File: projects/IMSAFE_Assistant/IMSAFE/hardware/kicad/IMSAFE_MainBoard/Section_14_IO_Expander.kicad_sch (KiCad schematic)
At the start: 6 parts, among them U16 MCP23017-E/SO

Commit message: Fix ERC errors across multiple schematic sections
- Section_04_BMS: Add VSYS hierarchical label for root schematic connection
- Section_05/06 Regulators: Add PWR_FLAG wire and junction to VSYS net
- Section_07_Barometric: Connect BMP390 SCK pin to GND for I2C mode
- Section_14_IO_Expander: Add no-connect symbols for unused MCP23017 GPIO pins
- Update design-rationale.md with ERC remediation status

Co-Authored-By: Claude Opus 4.5 <noreply@anthropic.com>
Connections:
- no-connect marks 0 -> 16
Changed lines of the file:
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@@
 	(wire (pts (xy 139.7 109.22) (xy 147.32 109.22)) (stroke (width 0) (type default)) (uuid "w-hl-inta"))
 	(wire (pts (xy 139.7 106.68) (xy 147.32 106.68)) (stroke (width 0) (type default)) (uuid "w-hl-intb"))
+	(no_connect (at 114.3 124.46) (uuid "nc-gpb0"))
+	(no_connect (at 114.3 121.92) (uuid "nc-gpb1"))
+	(no_connect (at 114.3 83.82) (uuid "nc-gpb2"))
+	(no_connect (at 114.3 86.36) (uuid "nc-gpb3"))
+	(no_connect (at 114.3 91.44) (uuid "nc-gpb4"))
+	(no_connect (at 114.3 93.98) (uuid "nc-gpb5"))
+	(no_connect (at 114.3 96.52) (uuid "nc-gpb6"))
+	(no_connect (at 114.3 99.06) (uuid "nc-gpb7"))
+	(no_connect (at 114.3 101.6) (uuid "nc-gpa0"))
+	(no_connect (at 114.3 104.14) (uuid "nc-gpa1"))
+	(no_connect (at 139.7 83.82) (uuid "nc-gpa2"))
+	(no_connect (at 139.7 86.36) (uuid "nc-gpa3"))
+	(no_connect (at 139.7 91.44) (uuid "nc-gpa4"))
+	(no_connect (at 139.7 93.98) (uuid "nc-gpa5"))
+	(no_connect (at 139.7 96.52) (uuid "nc-gpa6"))
+	(no_connect (at 139.7 99.06) (uuid "nc-gpa7"))
 	(sheet_instances (path "/" (page "1")))
 )

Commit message: Fix additional ERC errors in regulator and IO expander sections
- Section_05/06: Remove redundant PWR_FLAG on VSYS (BMS provides power_output)
- Section_14: Correct MCP23017 NC symbol positions to match actual pin coordinates

ERC reduction: 412 → 390 violations (22 fewer)
- Errors: 150 → 129 (-21)
- Warnings: 262 → 261 (-1)

Co-Authored-By: Claude Opus 4.5 <noreply@anthropic.com>
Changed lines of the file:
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@@
 	(no_connect (at 114.3 124.46) (uuid "nc-gpb0"))
 	(no_connect (at 114.3 121.92) (uuid "nc-gpb1"))
-	(no_connect (at 114.3 83.82) (uuid "nc-gpb2"))
-	(no_connect (at 114.3 86.36) (uuid "nc-gpb3"))
-	(no_connect (at 114.3 91.44) (uuid "nc-gpb4"))
-	(no_connect (at 114.3 93.98) (uuid "nc-gpb5"))
-	(no_connect (at 114.3 96.52) (uuid "nc-gpb6"))
-	(no_connect (at 114.3 99.06) (uuid "nc-gpb7"))
+	(no_connect (at 114.3 119.38) (uuid "nc-gpb2"))
+	(no_connect (at 114.3 116.84) (uuid "nc-gpb3"))
+	(no_connect (at 114.3 114.3) (uuid "nc-gpb4"))
+	(no_connect (at 114.3 111.76) (uuid "nc-gpb5"))
+	(no_connect (at 114.3 109.22) (uuid "nc-gpb6"))
+	(no_connect (at 114.3 106.68) (uuid "nc-gpb7"))
 	(no_connect (at 114.3 101.6) (uuid "nc-gpa0"))
-	(no_connect (at 114.3 104.14) (uuid "nc-gpa1"))
-	(no_connect (at 139.7 83.82) (uuid "nc-gpa2"))
-	(no_connect (at 139.7 86.36) (uuid "nc-gpa3"))
-	(no_connect (at 139.7 91.44) (uuid "nc-gpa4"))
-	(no_connect (at 139.7 93.98) (uuid "nc-gpa5"))
-	(no_connect (at 139.7 96.52) (uuid "nc-gpa6"))
-	(no_connect (at 139.7 99.06) (uuid "nc-gpa7"))
+	(no_connect (at 114.3 99.06) (uuid "nc-gpa1"))
+	(no_connect (at 114.3 96.52) (uuid "nc-gpa2"))
+	(no_connect (at 114.3 93.98) (uuid "nc-gpa3"))
+	(no_connect (at 114.3 91.44) (uuid "nc-gpa4"))
+	(no_connect (at 114.3 88.9) (uuid "nc-gpa5"))
+	(no_connect (at 114.3 86.36) (uuid "nc-gpa6"))
+	(no_connect (at 114.3 83.82) (uuid "nc-gpa7"))
 	(sheet_instances (path "/" (page "1")))
 )

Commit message: Add sensor and interface schematic implementations
- Section 01: MCU Core additional connections
- Section 04: BMS refinements
- Section 07: Barometric sensor (BMP390)
- Section 08: IMU (ICM-42688-P) full implementation
- Section 09: Magnetometer (MMC5983MA) full implementation
- Section 10: Gas sensor (MICS-4514) with heater control
- Section 11: Temp/Humidity (Si7021-A20) implementation
- Section 14: I/O Expander updates
- Section 16: Rotary encoder connections
- Section 19: Audio buzzer (MLT-8530) with MOSFET driver

Co-Authored-By: Claude Opus 4.5 <noreply@anthropic.com>
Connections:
- net +3V3: now also R1404.2
- net GND: now also R1401.2
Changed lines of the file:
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@@
 		(instances (project "IMSAFE_MainBoard" (path "/sec14-0001-0002-0003-000000000001" (reference "#PWR01404") (unit 1))))
+	)
+	(symbol (lib_id "power:+3V3") (at 167.64 111.76 90) (unit 1)
+		(exclude_from_sim no) (in_bom yes) (on_board yes) (dnp no)
+		(uuid "pwr-3v3-reset")
+		(property "Reference" "#PWR01405" (at 171.45 111.76 0) (effects (font (size 1.27 1.27)) hide))
+		(property "Value" "+3V3" (at 172.72 111.76 0) (effects (font (size 1.27 1.27))))
+		(property "Footprint" "" (at 167.64 111.76 0) (effects (font (size 1.27 1.27)) hide))
+		(property "Datasheet" "" (at 167.64 111.76 0) (effects (font (size 1.27 1.27)) hide))
+		(pin "1" (uuid "pwr-3v3-reset-p1"))
+		(instances (project "IMSAFE_MainBoard" (path "/sec14-0001-0002-0003-000000000001" (reference "#PWR01405") (unit 1))))
 	)
 	(wire (pts (xy 127 71.12) (xy 127 78.74)) (stroke (width 0) (type default)) (uuid "w-3v3-vdd"))
@@
 	(wire (pts (xy 160.02 92.71) (xy 160.02 96.52)) (stroke (width 0) (type default)) (uuid "w-c1401-gnd"))
 	(wire (pts (xy 139.7 111.76) (xy 151.13 111.76)) (stroke (width 0) (type default)) (uuid "w-reset-r1404"))
-	(wire (pts (xy 158.75 111.76) (xy 165.1 111.76)) (stroke (width 0) (type default)) (uuid "w-r1404-3v3"))
+	(wire (pts (xy 158.75 111.76) (xy 167.64 111.76)) (stroke (width 0) (type default)) (uuid "w-r1404-3v3"))
 	(wire (pts (xy 139.7 88.9) (xy 151.13 88.9)) (stroke (width 0) (type default)) (uuid "w-a0-r1401"))
 	(wire (pts (xy 158.75 88.9) (xy 165.1 88.9)) (stroke (width 0) (type default)) (uuid "w-r1401-gnd"))
@@
 	(wire (pts (xy 139.7 124.46) (xy 151.13 124.46)) (stroke (width 0) (type default)) (uuid "w-a2-r1403"))
 	(wire (pts (xy 158.75 124.46) (xy 165.1 124.46)) (stroke (width 0) (type default)) (uuid "w-r1403-gnd"))
-	(wire (pts (xy 165.1 88.9) (xy 165.1 111.76)) (stroke (width 0) (type default)) (uuid "w-gnd-tie1"))
+	(wire (pts (xy 165.1 88.9) (xy 165.1 121.92)) (stroke (width 0) (type default)) (uuid "w-gnd-tie1"))
 	(wire (pts (xy 165.1 121.92) (xy 165.1 124.46)) (stroke (width 0) (type default)) (uuid "w-gnd-tie2"))
 	(hierarchical_label "I2C1_SDA" (shape bidirectional) (at 147.32 119.38 0) (fields_autoplaced yes)

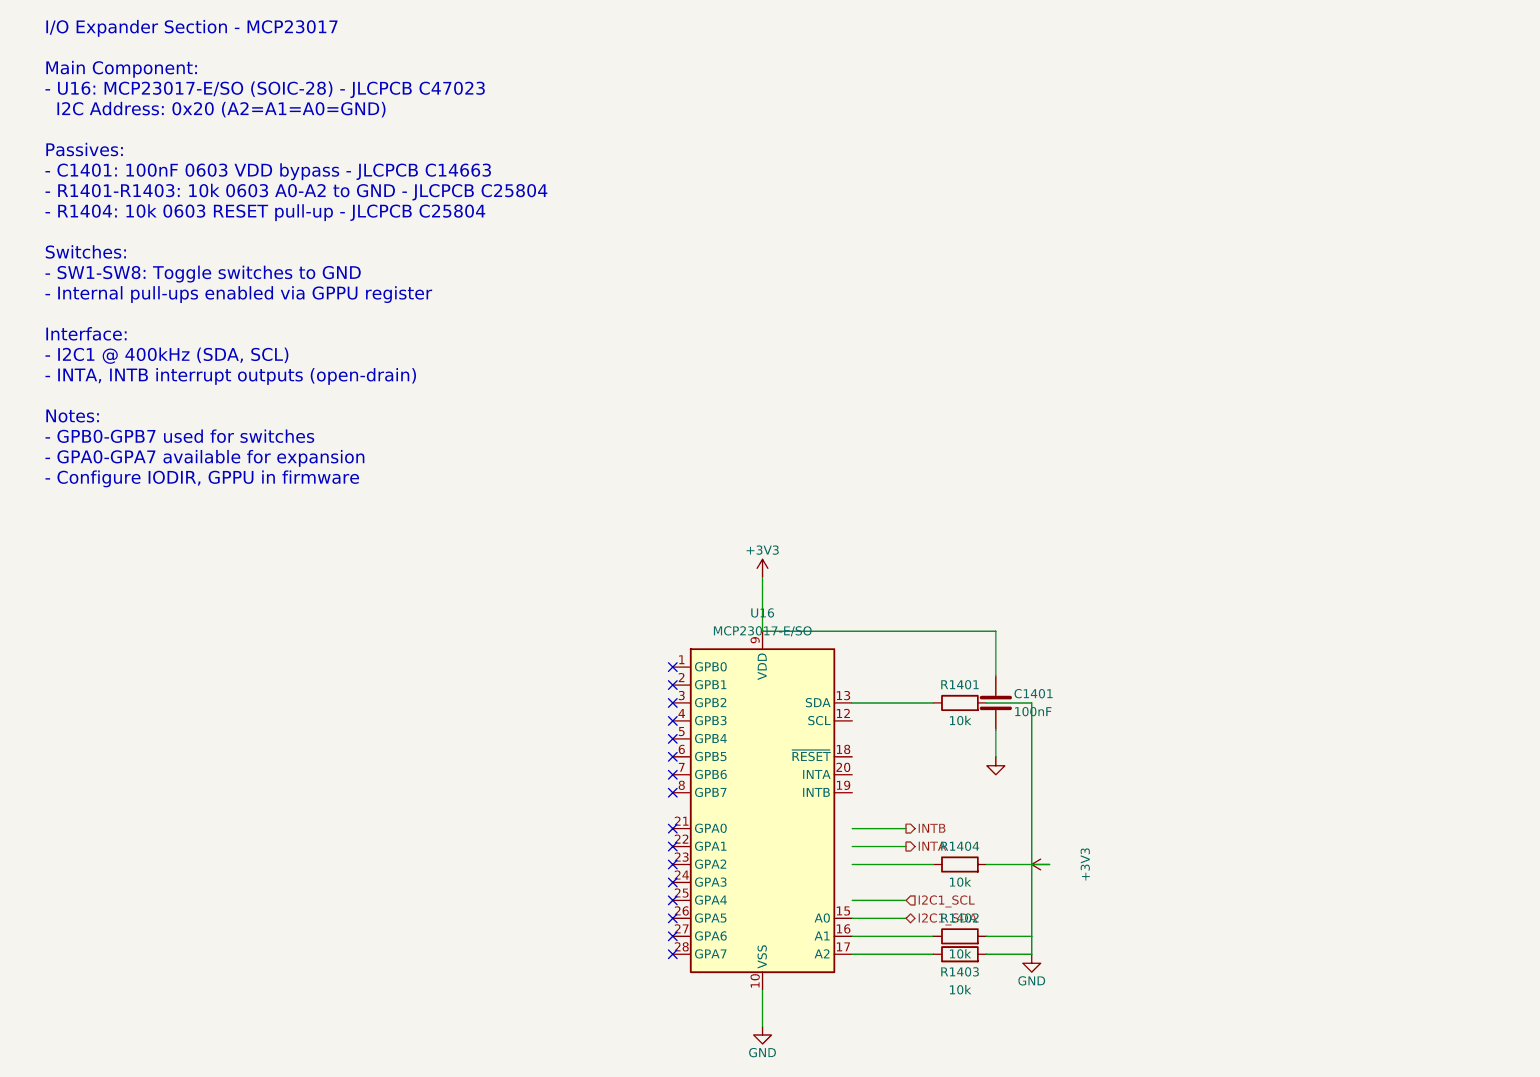
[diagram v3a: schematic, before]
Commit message: Update KiCad schematics and add analysis files
- Update all MainBoard schematic sections with component placement
- Add ERC reports and analysis scripts for schematic validation
- Update Radar Interface and SwitchLED Board projects
- Sync KiCad project files with latest session changes

Co-Authored-By: Claude Opus 4.5 <noreply@anthropic.com>
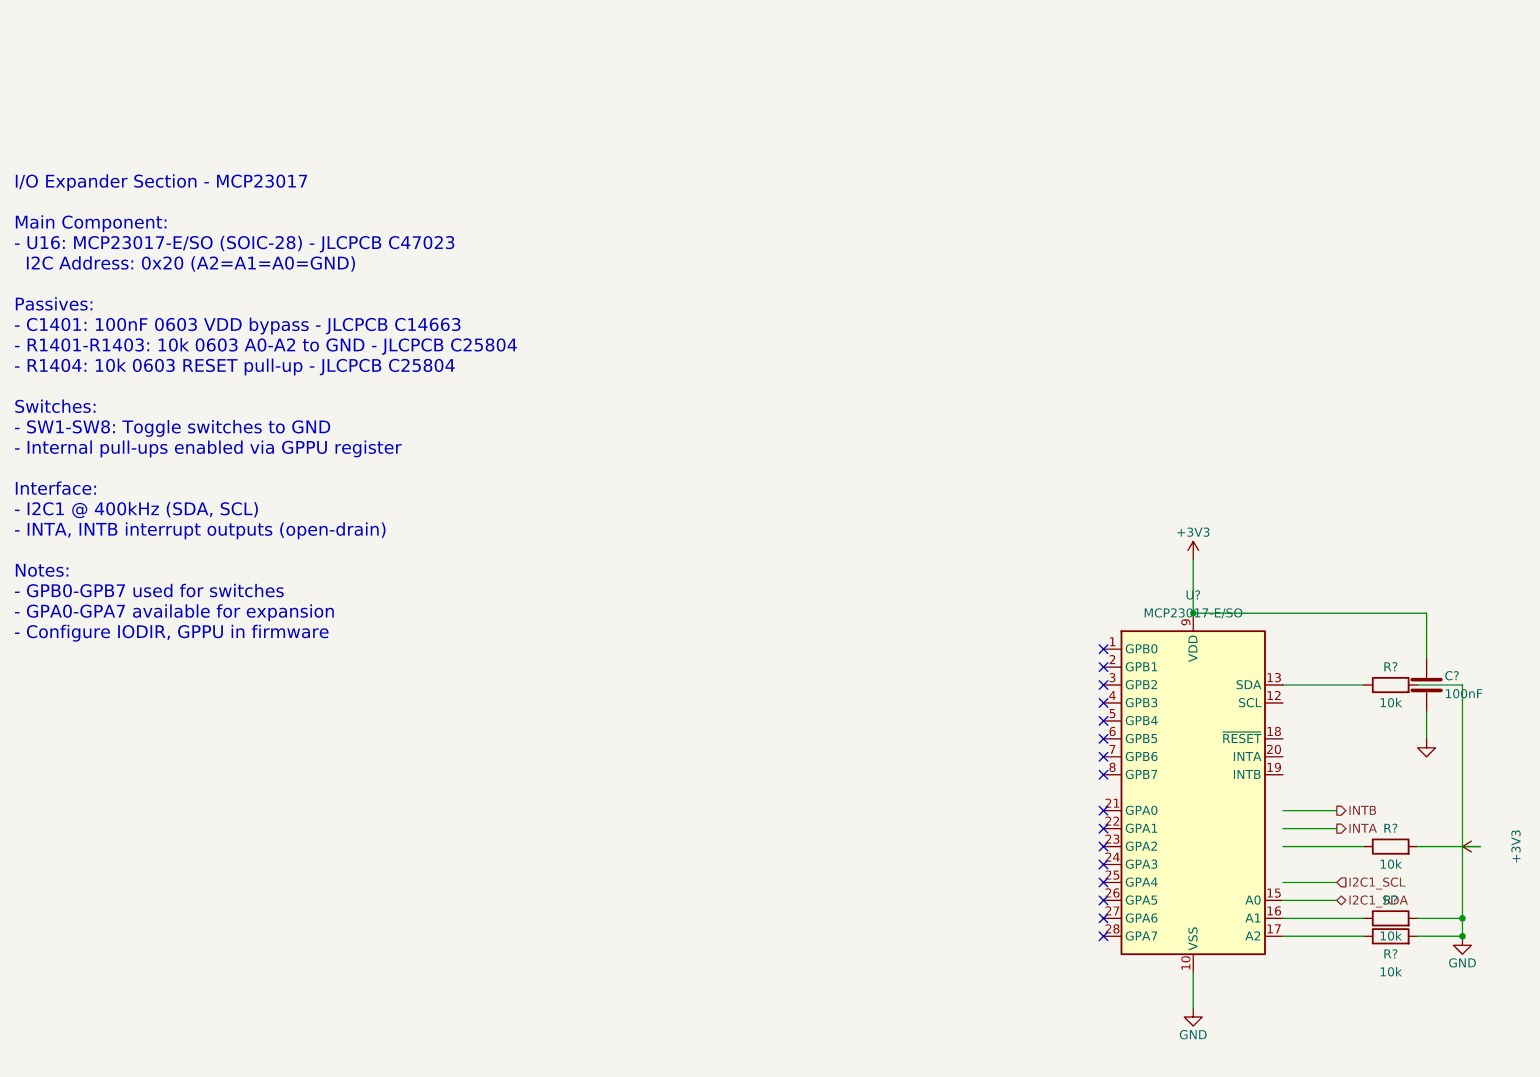
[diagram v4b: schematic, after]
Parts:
- removed C1401: 100nF, Capacitor_SMD:C_0603_1608Metric, symbol Device:C
- removed R1401, R1402, R1403, R1404: 10k, Resistor_SMD:R_0603_1608Metric, symbol Device:R
- removed U16: MCP23017-E/SO, Package_SO:SOIC-28W_7.5x17.9mm_P1.27mm, symbol Interface_Expansion:MCP23017
- added C?: 100nF, Capacitor_SMD:C_0603_1608Metric, symbol Device:C
- added R? (x4): 10k, Resistor_SMD:R_0603_1608Metric, symbol Device:R
- added U?: MCP23017-E/SO, Package_SO:SOIC-28W_7.5x17.9mm_P1.27mm, symbol Interface_Expansion:MCP23017
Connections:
- net +3V3: now also C?.1, R?.2, U?.9 (VDD)
- net GND: now also C?.2, R?.2, R?.2, R?.2, U?.10 (VSS)
- net I2C1_SDA: now also U?.15 (A0)
- new net: R?.1, U?.17 (A2)
- new net: R?.1, U?.13 (SDA)
- new net: R?.1, U?.16 (A1)
